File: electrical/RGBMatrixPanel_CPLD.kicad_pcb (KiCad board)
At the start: 2 copper layers, 71.1 x 50.8 mm, 28 parts, among them J1 BARREL_JACK, J2 CONN_01X01, J3 CONN_01X01, J4 CONN_01X01, J5 CONN_01X01, J6 CONN_01X06, J7 CONN_02X08, J8 CONN_01X06, Q1 Photo_Trans, U1 PHOTON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

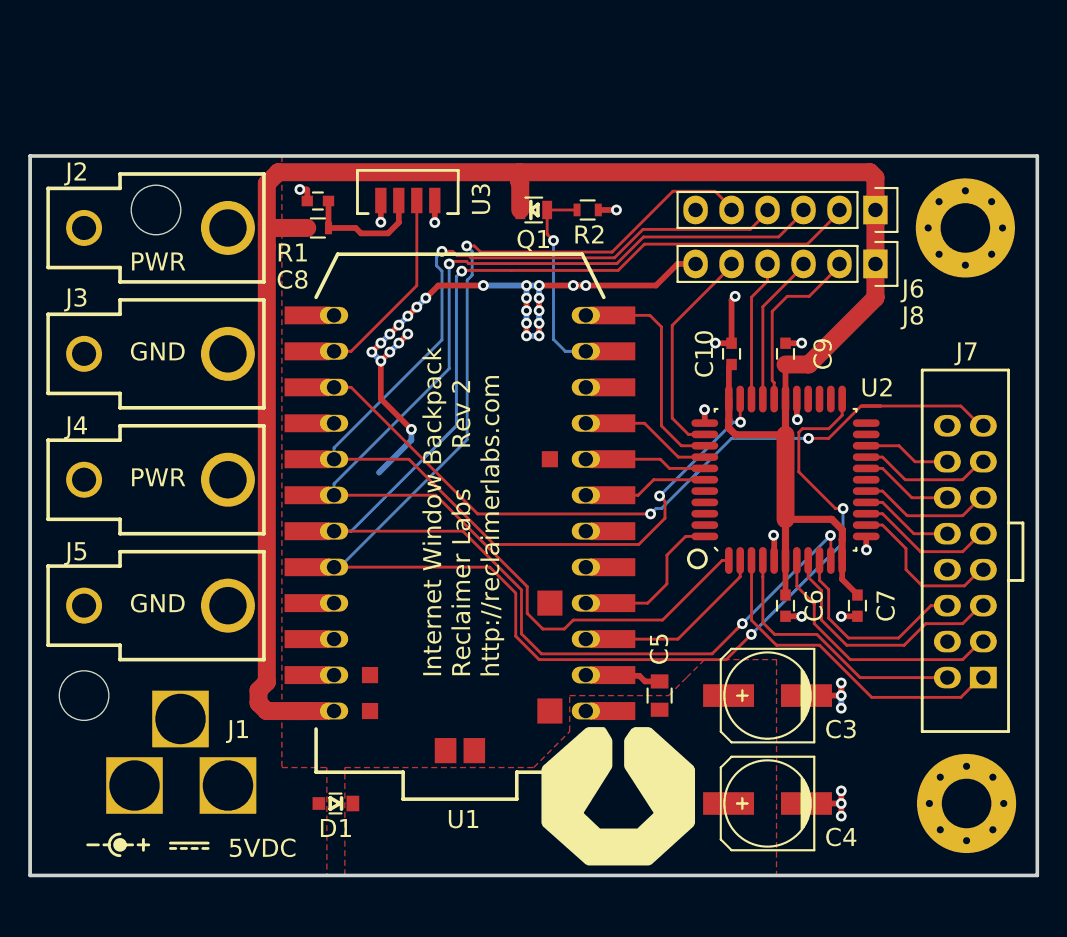
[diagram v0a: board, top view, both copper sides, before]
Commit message: Rev 3
Updates include new board outline to accomendate mounting to sheet metal
frame
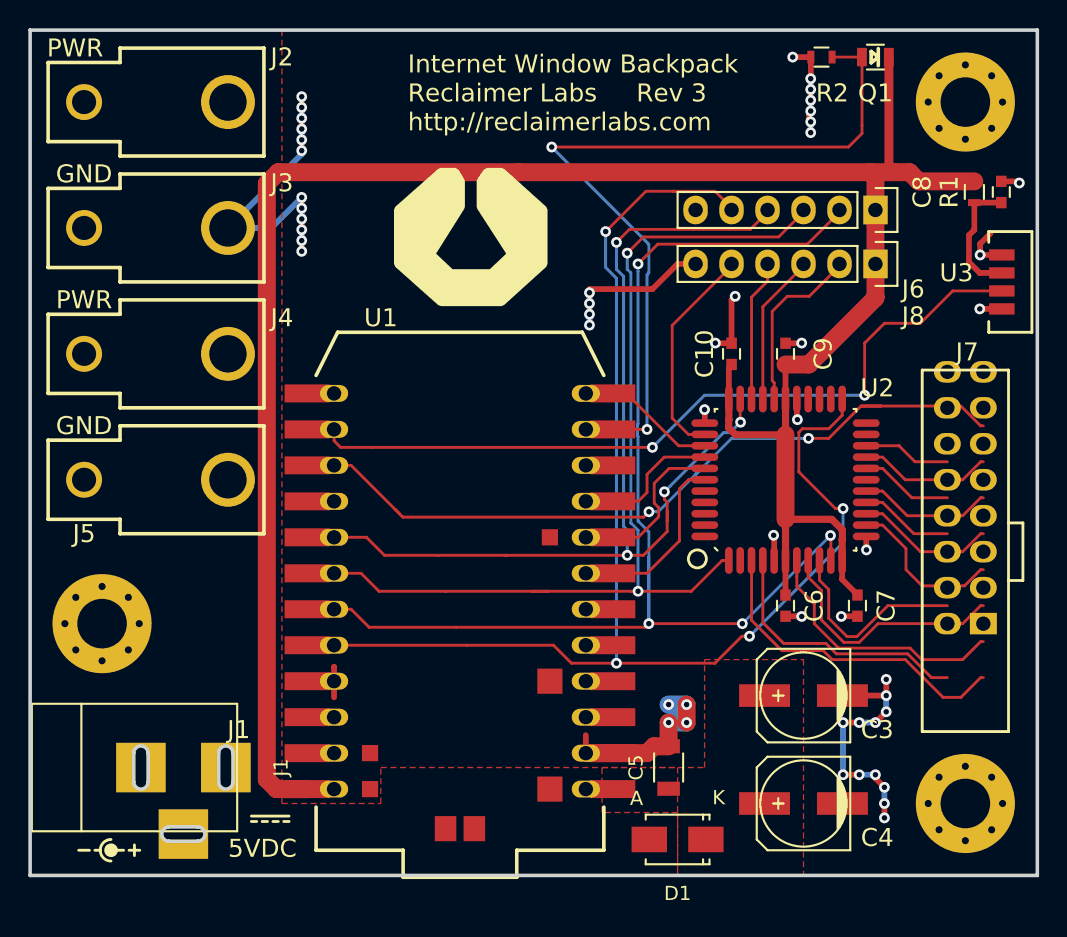
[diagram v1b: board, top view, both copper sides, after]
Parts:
- removed X4: MTHOLE, Reclaimer_Labs:MountingHole_3.5mm_Pad_Via
- C5: footprint Capacitors_SMD:C_0805 -> Capacitors_SMD:C_1206
- D1: footprint Reclaimer_Labs:SMini2-F5-B -> Reclaimer_Labs:SMA
- J1: footprint Reclaimer_Labs:BARREL_JACK_MPD_EJ508A -> Reclaimer_Labs:BARREL_JACK_PJ_202AH_Slots; moved to F.Cu
- U3: value TSOP75238TT -> TSSP77P38TTR
- X1, X2: footprint Mounting_Holes:MountingHole_3.5mm -> Reclaimer_Labs:MountingHole_3.5mm_Pad_Via
- moved X2 70.9 mm to (116.8, 111.8)
- moved C8 48.3 mm to (119.4, 68.6), turned to 90 degrees
- moved R1 46.4 mm to (117.5, 68.6), turned to 270 degrees
- moved U3 43.0 mm to (120.0, 74.9), turned to 270 degrees
- moved G*** 40.8 mm to (81.9, 71.8)
- moved Q1 26.4 mm to (110.5, 59.1), turned to 0 degrees
- moved D1 24.3 mm to (96.5, 114.3)
- moved R2 19.7 mm to (106.7, 59.1), turned to 180 degrees
- moved J2 8.89 mm to (59.7, 62.2)
- moved X3 8.89 mm to (116.8, 62.2)
- moved J3 8.89 mm to (59.7, 71.1)
- moved J4 8.89 mm to (59.7, 80.0)
- moved J5 8.89 mm to (59.7, 88.9)
- moved U1 5.51 mm to (81.2, 96.8)
- moved X1 5.24 mm to (55.9, 99.1)
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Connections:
- U2 pad 2: /UART_TX -> Net-(U2-Pad2)
- U2 pad 44: /UART_RX -> Net-(U2-Pad44)
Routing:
- net /IRDA: track 15.7 -> 56.8 mm, vias 0 -> 2
- net /PHOTO: track 16.0 -> 57.0 mm, vias 1 -> 2
- net +3V3: track 143.9 -> 157.7 mm
- net /TDI: track 83.3 -> 70.7 mm, vias 1 -> 2
- net /TCK: track 100.4 -> 88.3 mm, vias 3 -> 4
- net /UART_TX: track 13.9 -> 1.91 mm
- net /TMS: track 108.3 -> 97.6 mm, vias 3 -> 4
- net GND: track 83.3 -> 92.8 mm, vias 44 -> 51
- net /UART_RX: track 11.5 -> 2.24 mm
- net /TDO: track 82.6 -> 73.6 mm, vias 3 -> 4
- net /RST_CPLD: track 16.3 -> 9.93 mm
- net /SPI_MOSI: track 8.85 -> 15.2 mm
- net /SPI_MISO: track 8.67 -> 12.2 mm
- net /OE: track 56.9 -> 55.2 mm
- net /SPI_SCK: track 9.39 -> 10.4 mm
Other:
- board size 71.1 x 50.8 mm -> 71.1 x 59.7 mm
- board text added: "Internet Window Backpack Reclaimer Labs Rev 3 http://reclaimerlabs.com"
- board text removed: "Internet Window Backpack Reclaimer Labs Rev 2 http://reclaimerlabs.com"

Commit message: moved mounting hole
Moved mounting hole to better align with the sheet metal frame
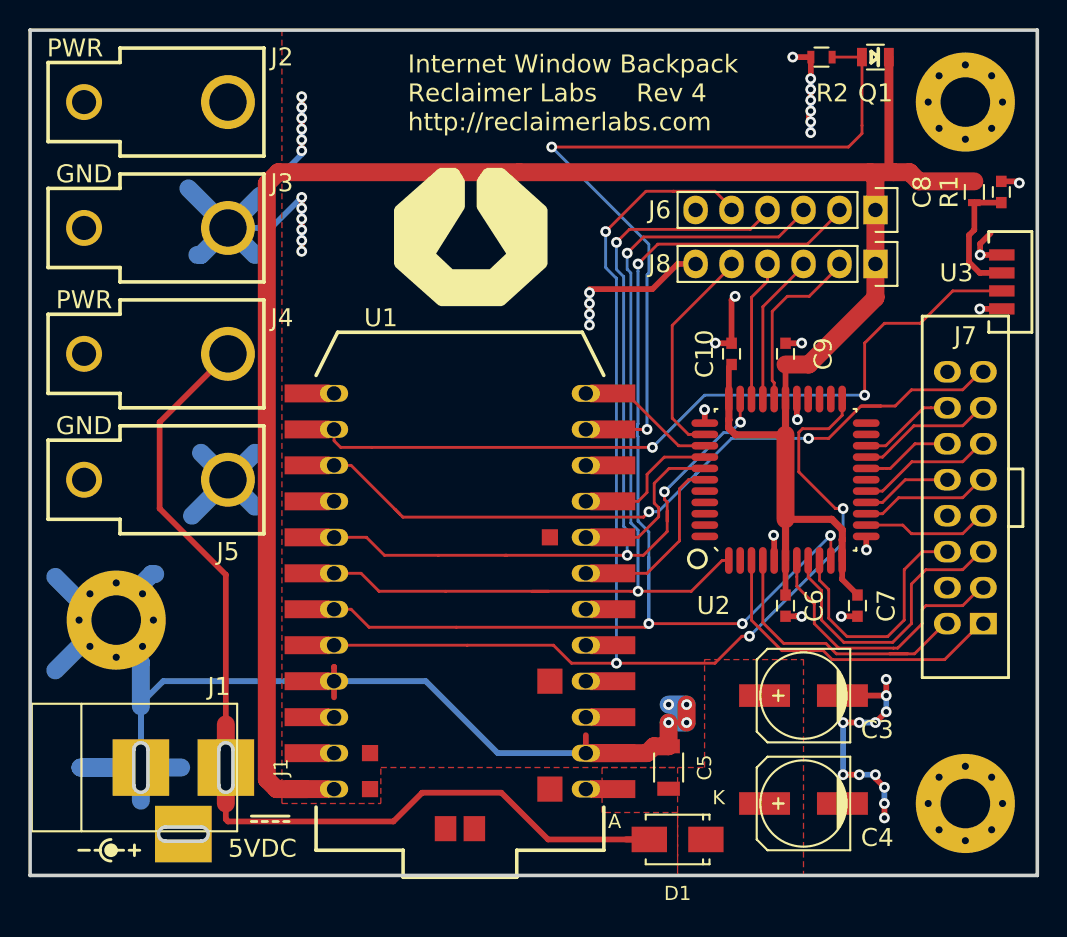
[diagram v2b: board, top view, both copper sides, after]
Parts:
- moved X1 1.03 mm to (56.9, 98.8)
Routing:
- net GND: track 92.8 -> 192.3 mm
- net +5V: track 0.00 -> 70.6 mm
- net /G2: track 14.2 -> 17.8 mm
- net /R2: track 17.8 -> 21.0 mm
- net /B2: track 11.4 -> 9.05 mm
- net /B1: track 18.5 -> 20.0 mm
- net /G1: track 19.0 -> 20.5 mm
- net /D: track 6.59 -> 7.60 mm
- net /A: track 9.91 -> 9.26 mm
- net /LAT: track 6.20 -> 6.84 mm
- net /R1: track 23.4 -> 22.8 mm
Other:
- outline, holes or cut-outs redrawn
- board text added: "Internet Window Backpack Reclaimer Labs Rev 4 http://reclaimerlabs.com"
- board text removed: "Internet Window Backpack Reclaimer Labs Rev 3 http://reclaimerlabs.com"

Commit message: Rev 5
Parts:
- removed D1: D_Schottky, Reclaimer_Labs:SMA
- added C1: 4.7uF, Capacitors_SMD:C_1206, B.Cu at (81.3, 109.2)
- added C11: 0.47uF, Capacitors_SMD:C_0805, B.Cu at (83.7, 102.6)
- added C12: 1.0uF, Capacitors_SMD:C_0603, B.Cu at (75.4, 108.4)
- added C13: 390pF, Capacitors_SMD:C_0603, B.Cu at (66.7, 101.6)
- added C14: 100uF, Capacitors_SMD:C_1206, B.Cu at (79.2, 97.0)
- added C15: DNP, Capacitors_SMD:C_1206, B.Cu at (76.7, 97.0)
- added C2: 4.7uF, Capacitors_SMD:C_1206, B.Cu at (83.8, 109.2)
- added J9: CONN_01X03, Socket_Strips:Socket_Strip_Straight_1x03, F.Cu at (119.4, 68.6)
- added L1: 2.2uH, Reclaimer_Labs:SRR1270, B.Cu at (89.4, 90.2)
- added Q2: CSD17307Q5A, Reclaimer_Labs:MOSFET_Q5A, B.Cu at (94.5, 101.8)
- added Q3: CSD18531Q5A, Reclaimer_Labs:MOSFET_Q5A, B.Cu at (88.1, 101.8)
- added R3: 73k2, Capacitors_SMD:C_0603, B.Cu at (64.8, 101.6)
- added R4: 1k69, Capacitors_SMD:C_0603, B.Cu at (83.0, 98.9)
- added R5: 73k2, Capacitors_SMD:C_0603, B.Cu at (68.6, 101.6)
- added R6: 10k, Capacitors_SMD:C_0603, B.Cu at (70.5, 101.6)
- C10, C6, C7, C9, U2: moved to B.Cu
- C3: value 100uF -> 4.7uF; footprint Capacitors_SMD:c_elec_6.3x5.7 -> Capacitors_SMD:C_1206; moved to B.Cu
- C4: value 100uF -> 0.1uF; footprint Capacitors_SMD:c_elec_6.3x5.7 -> Capacitors_SMD:C_0805; moved to B.Cu
- C5: value 10uF -> 0.01uF; footprint Capacitors_SMD:C_1206 -> Capacitors_SMD:C_0603; moved to B.Cu
- R1, R2: footprint Resistors_SMD:R_0603 -> Capacitors_SMD:C_0603
- U3: value TSSP77P38TTR -> LM3150; footprint Reclaimer_Labs:TSOP75238TT -> Reclaimer_Labs:TSSOP-14-0.65mm-EP; moved to B.Cu
- moved U3 50.7 mm to (78.0, 103.3), turned to 90 degrees
- moved Q1 46.6 mm to (119.4, 104.8), turned to 270 degrees
- moved R2 46.2 mm to (116.8, 104.1)
- moved J6 44.5 mm to (110.5, 114.3), turned to 90 degrees
- moved J8 40.7 mm to (108.0, 114.3), turned to 90 degrees
- moved C7 40.5 mm to (85.7, 64.8), turned to 90 degrees
- moved U1 29.3 mm to (94.0, 70.5), turned to 0 degrees
- moved C6 27.8 mm to (101.7, 70.1), turned to 90 degrees
- moved C5 24.7 mm to (72.4, 101.6)
- moved U2 21.3 mm to (93.3, 70.5), turned to 0 degrees
- moved C3 19.7 mm to (86.4, 109.2), turned to 90 degrees
- moved G*** 18.9 mm to (77.5, 90.2)
- moved C10 17.6 mm to (85.1, 71.1), turned to 270 degrees
- moved C4 16.1 mm to (89.5, 109.2), turned to 90 degrees
- moved R1 5.24 mm to (116.2, 73.7), turned to 0 degrees
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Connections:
- net /BUZZER_BOT renamed Net-(U1-Pad13)
- net /BUZZER_TOP renamed Net-(U1-Pad6)
- C3 pad 1: +5VA -> VIN
- C4 pad 1: +5VA -> VIN
- C5 pad 1: +5VA -> /SS
- C8 pad 1: Net-(C8-Pad1) -> /IR_PWR
- J1 pad 1: +5V -> VIN
- J8 pad 2: /CPLD_B8 -> /CPLD_A3
- J8 pad 3: /CPLD_B9 -> /CPLD_A2
- J8 pad 4: /CPLD_B10 -> /CPLD_A1
- J8 pad 5: /CPLD_B12 -> /CPLD_A0
- R1 pad 2: Net-(C8-Pad1) -> /IR_PWR
- U1 pad 1: +5VA -> +5V
- U1 pad 10: /PHOTON_A2 -> /TDO
- U1 pad 16: /PHOTON_D3 -> /TMS
- U1 pad 17: /TDO -> Net-(U1-Pad17)
- U1 pad 20: /TMS -> Net-(U1-Pad20)
- U2 pad 13: /B2 -> Net-(U2-Pad13)
- U2 pad 14: /A -> Net-(U2-Pad14)
- U2 pad 15: /B -> Net-(U2-Pad15)
- U2 pad 16: /C -> /CLK
- U2 pad 18: /D -> /LAT
- U2 pad 19: /CLK -> /C
- U2 pad 20: /LAT -> /D
- U2 pad 21: Net-(U2-Pad21) -> /A
- U2 pad 22: Net-(U2-Pad22) -> /B
- U2 pad 24: Net-(U2-Pad24) -> /B2
- U2 pad 25: Net-(U2-Pad25) -> /R2
- U2 pad 26: Net-(U2-Pad26) -> /G2
- U2 pad 29: /CPLD_B8 -> /B1
- U2 pad 3: /R1 -> Net-(U2-Pad3)
- U2 pad 30: /CPLD_B9 -> /R1
- U2 pad 31: /CPLD_B10 -> /G1
- U2 pad 35: /CPLD_B12 -> Net-(U2-Pad35)
- U2 pad 4: /G1 -> Net-(U2-Pad4)
- U2 pad 40: Net-(U2-Pad40) -> /CPLD_A0
- U2 pad 41: Net-(U2-Pad41) -> /CPLD_A1
- U2 pad 42: Net-(U2-Pad42) -> /CPLD_A2
- U2 pad 43: Net-(U2-Pad43) -> /CPLD_A3
- U2 pad 7: /B1 -> Net-(U2-Pad7)
- U2 pad 8: /R2 -> Net-(U2-Pad8)
- U2 pad 9: /G2 -> Net-(U2-Pad9)
- U3 pad 1: GND -> /VCC
- U3 pad 2: Net-(C8-Pad1) -> VIN
- U3 pad 3: /IRDA -> Net-(U3-Pad3)
- U3 pad 4: GND -> /FB
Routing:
- net GND: track 192.3 -> 254.1 mm, vias 51 -> 63
- net /CPLD_A3: track 0.00 -> 48.9 mm
- net /CPLD_A2: track 0.00 -> 47.1 mm
- net +5V: track 70.6 -> 24.2 mm
- net +3V3: track 157.7 -> 113.4 mm, vias 0 -> 7
- net /CPLD_A1: track 0.00 -> 42.8 mm
- net /TMS: track 97.6 -> 57.2 mm, vias 4 -> 2
- net /CPLD_A0: track 0.00 -> 39.8 mm
- net /CLK: track 9.71 -> 48.6 mm
- net /LAT: track 6.84 -> 44.3 mm
- net /A: track 9.26 -> 41.1 mm
- net /C: track 9.65 -> 40.8 mm
- net /B: track 6.39 -> 36.3 mm
- net /D: track 7.60 -> 37.4 mm
- net /B2: track 9.05 -> 38.5 mm
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- added copper zone on B.Cu, net +3V3
- added copper zone on B.Cu, net +5V
- added copper zone on B.Cu, net /SW
- added copper zone on B.Cu, net VIN
- removed copper zone on F.Cu, net +5V
- removed copper zone on F.Cu, net +5VA
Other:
- net class Default: clearance 0.2032 -> 0.12446; trace_width 0.2032 -> 0.127
- net class Power: clearance 0.2032 -> 0.12446; trace_width 0.4064 -> 0.254
- rule trace_clearance: 0.2032 -> 0.12446
- rule trace_min: 0.2032 -> 0.12446
- board text added: "3V3"
- board text added: "A0"
- board text added: "A1"
- board text added: "A2"
- board text added: "A3"
- board text added: "CPLD"
- board text added: "IRDA"
- board text added: "Internet Window Backpack Reclaimer Labs Rev 5 http://reclaimerlabs.com"
- board text added: "TCK"
- board text added: "TDI"
- board text added: "TDO"
- board text added: "TMS"
- board text removed: "5VDC"
- board text removed: "Internet Window Backpack Reclaimer Labs Rev 4 http://reclaimerlabs.com"
- board text removed: "J1"
- board text removed: "J7"
